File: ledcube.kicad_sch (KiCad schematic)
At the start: 0 parts

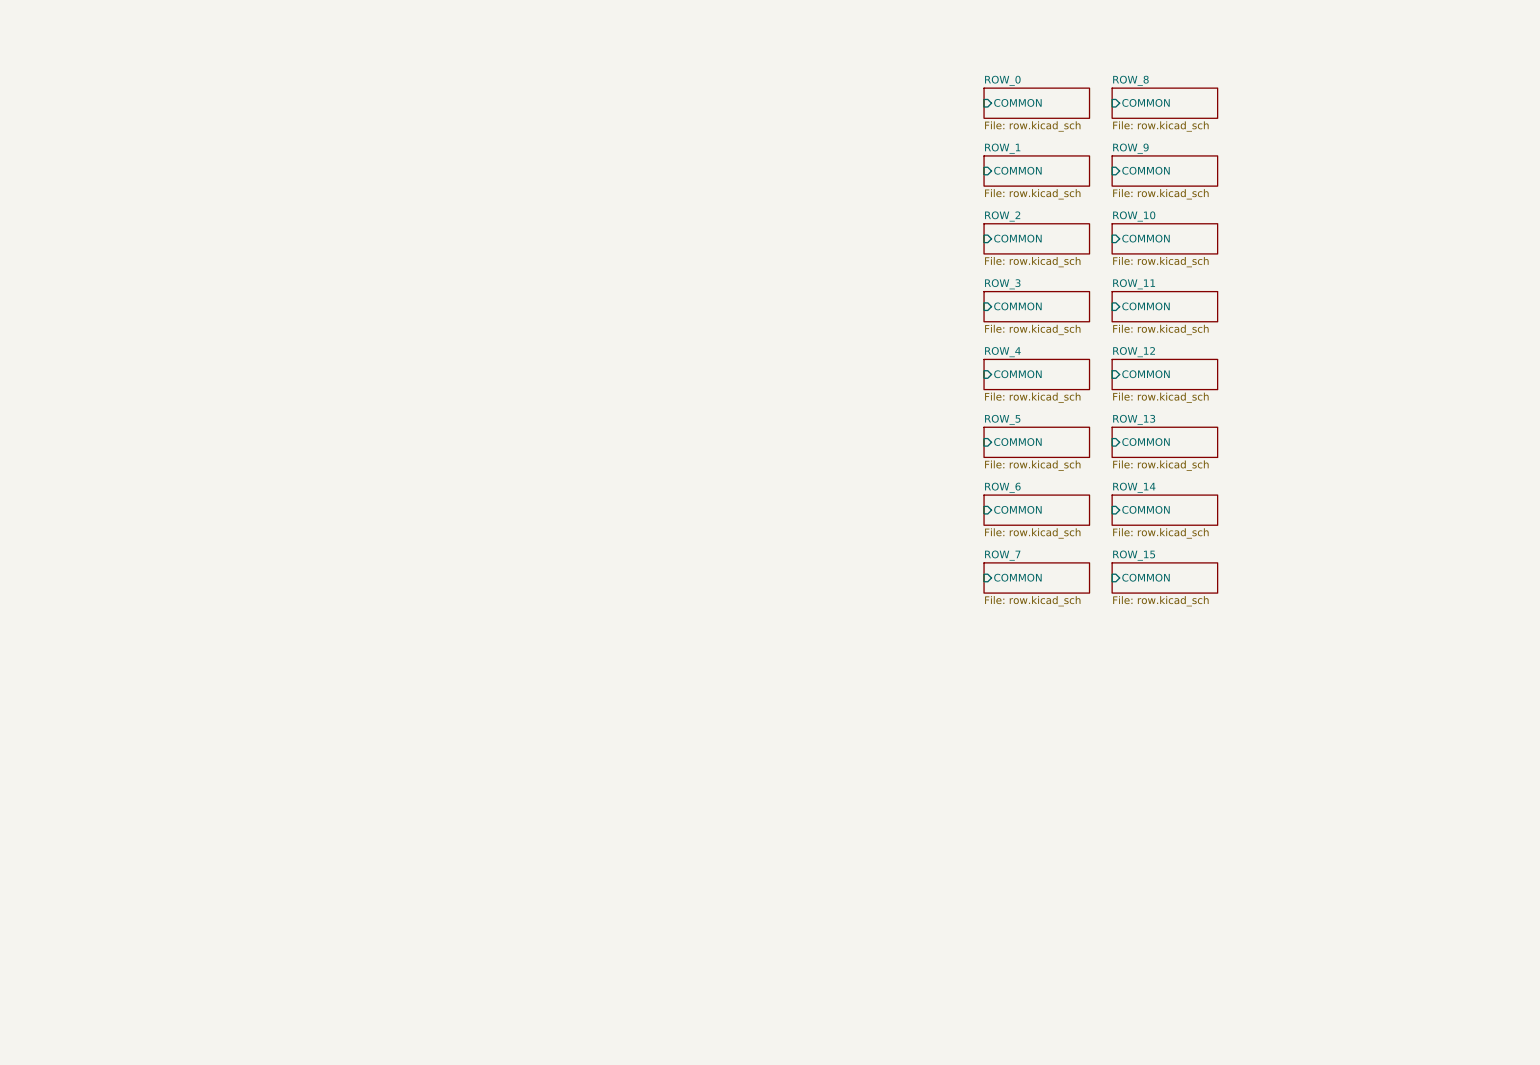
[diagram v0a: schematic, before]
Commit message: Row/column labels attached to shift registers/drivers
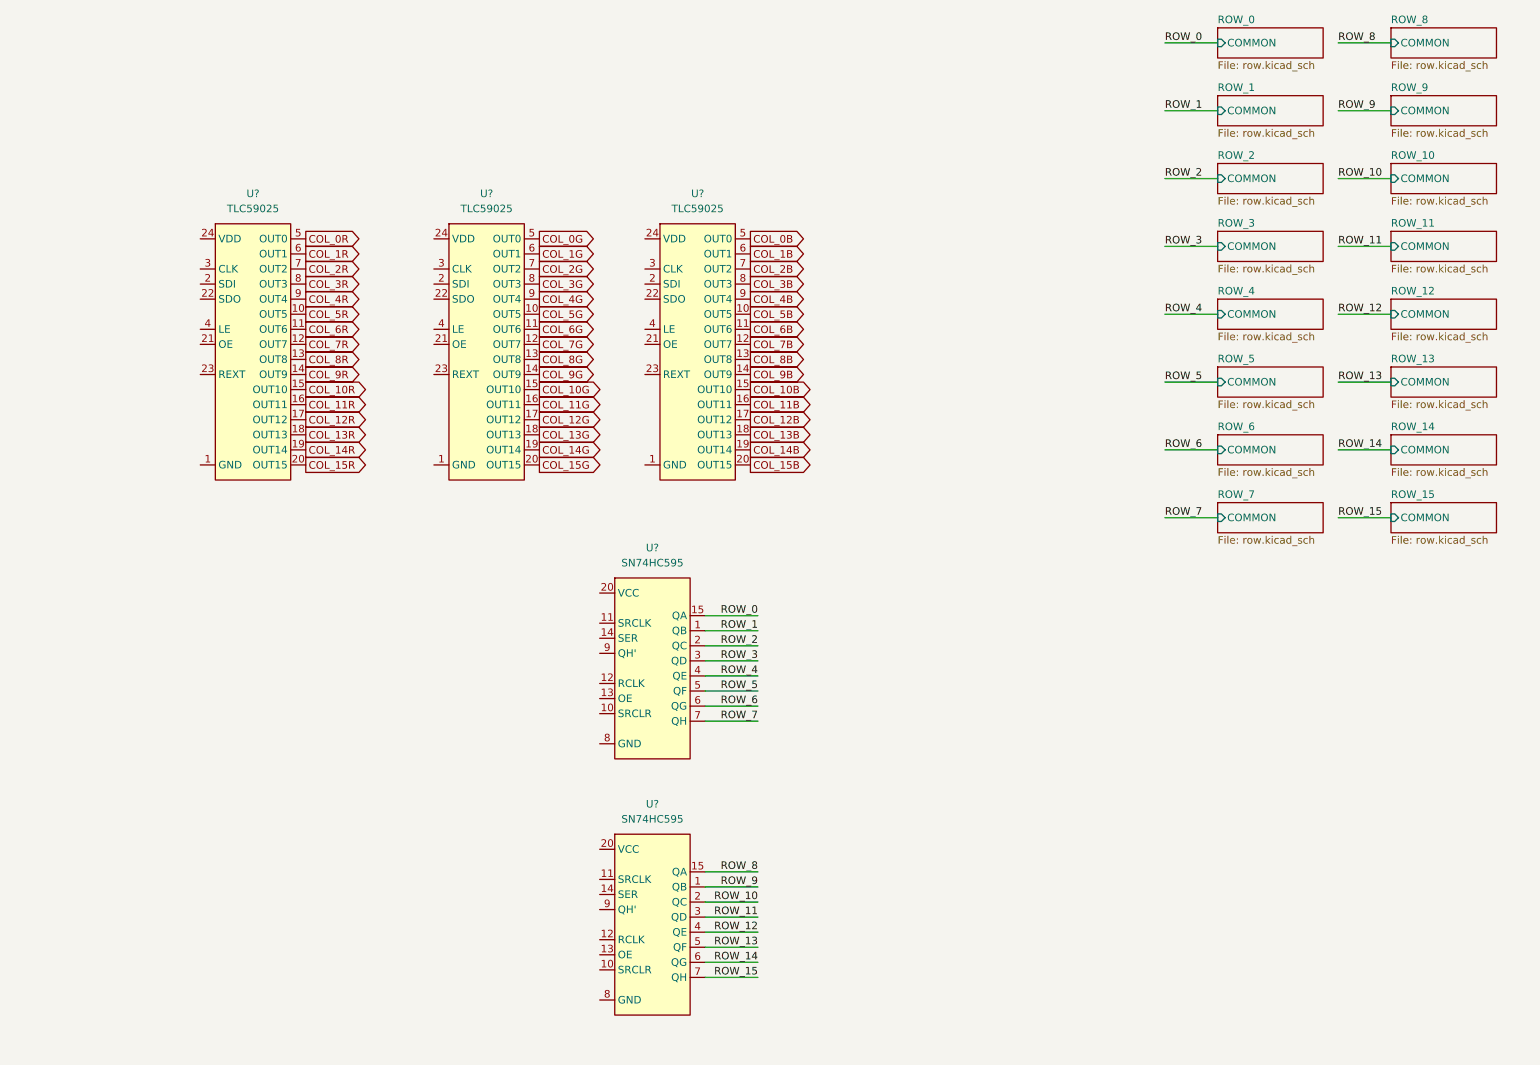
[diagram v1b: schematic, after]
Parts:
- added U? (x2): SN74HC595, symbol ledcube:SN74HC595
- added U? (x3): TLC59025, symbol ledcube:TLC59025
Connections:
- new net COL_0B: U?.5 (OUT0)
- new net COL_0G: U?.5 (OUT0)
- new net COL_0R: U?.5 (OUT0)
- new net COL_10B: U?.15 (OUT10)
- new net COL_10G: U?.15 (OUT10)
- new net COL_10R: U?.15 (OUT10)
- new net COL_11B: U?.16 (OUT11)
- new net COL_11G: U?.16 (OUT11)
- new net COL_11R: U?.16 (OUT11)
- new net COL_12B: U?.17 (OUT12)
- new net COL_12G: U?.17 (OUT12)
- new net COL_12R: U?.17 (OUT12)
- new net COL_13B: U?.18 (OUT13)
- new net COL_13G: U?.18 (OUT13)
- new net COL_13R: U?.18 (OUT13)
- new net COL_14B: U?.19 (OUT14)
- new net COL_14G: U?.19 (OUT14)
- new net COL_14R: U?.19 (OUT14)
- new net COL_15B: U?.20 (OUT15)
- new net COL_15G: U?.20 (OUT15)
- new net COL_15R: U?.20 (OUT15)
- new net COL_1B: U?.6 (OUT1)
- new net COL_1G: U?.6 (OUT1)
- new net COL_1R: U?.6 (OUT1)
- new net COL_2B: U?.7 (OUT2)
- new net COL_2G: U?.7 (OUT2)
- new net COL_2R: U?.7 (OUT2)
- new net COL_3B: U?.8 (OUT3)
- new net COL_3G: U?.8 (OUT3)
- new net COL_3R: U?.8 (OUT3)
- new net COL_4B: U?.9 (OUT4)
- new net COL_4G: U?.9 (OUT4)
- new net COL_4R: U?.9 (OUT4)
- new net COL_5B: U?.10 (OUT5)
- new net COL_5G: U?.10 (OUT5)
- new net COL_5R: U?.10 (OUT5)
- new net COL_6B: U?.11 (OUT6)
- new net COL_6G: U?.11 (OUT6)
- new net COL_6R: U?.11 (OUT6)
- new net COL_7B: U?.12 (OUT7)
- new net COL_7G: U?.12 (OUT7)
- new net COL_7R: U?.12 (OUT7)
- new net COL_8B: U?.13 (OUT8)
- new net COL_8G: U?.13 (OUT8)
- new net COL_8R: U?.13 (OUT8)
- new net COL_9B: U?.14 (OUT9)
- new net COL_9G: U?.14 (OUT9)
- new net COL_9R: U?.14 (OUT9)
- new net ROW_0: U?.15 (QA)
- new net ROW_1: U?.1 (QB)
- new net ROW_10: U?.2 (QC)
- new net ROW_11: U?.3 (QD)
- new net ROW_12: U?.4 (QE)
- new net ROW_13: U?.5 (QF)
- new net ROW_14: U?.6 (QG)
- new net ROW_15: U?.7 (QH)
- new net ROW_2: U?.2 (QC)
- new net ROW_3: U?.3 (QD)
- new net ROW_4: U?.4 (QE)
- new net ROW_5: U?.5 (QF)
- new net ROW_6: U?.6 (QG)
- new net ROW_7: U?.7 (QH)
- new net ROW_8: U?.15 (QA)
- new net ROW_9: U?.1 (QB)

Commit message: PMOS drivers, buffers, and serial connections
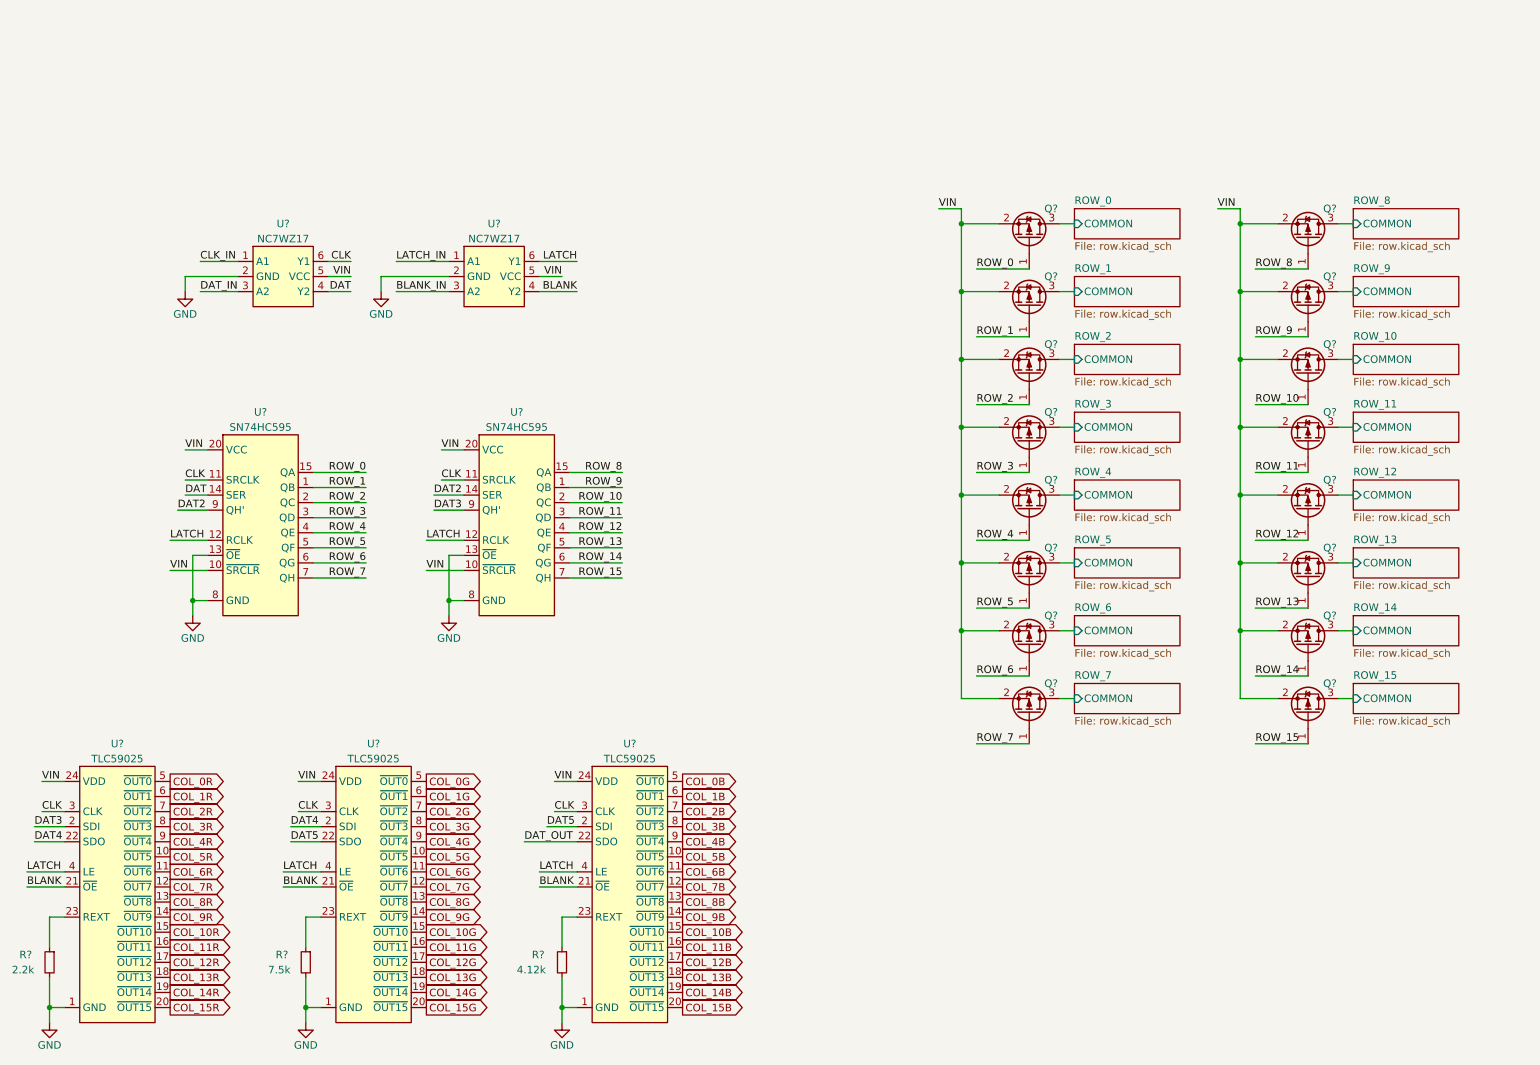
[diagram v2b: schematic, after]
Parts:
- added Q? (x16): Q_PMOS_GSD, symbol Device:Q_PMOS_GSD
- added R?: 7.5k, symbol Device:R_Small
- added R?: 2.2k, symbol Device:R_Small
- added R?: 4.12k, symbol Device:R_Small
- added U? (x2): NC7WZ17, Package_SON:Fairchild_MicroPak2-6_1.0x1.0mm_P0.35mm, symbol ledcube:NC7WZ17
- U? (x2): footprint (none) -> Package_SO:TSSOP-16_4.4x5mm_P0.65mm; MPN (none) -> SN74HC595PWR
- U? (x3): footprint (none) -> Package_SO:SSOP-24_3.9x8.7mm_P0.635mm; MPN (none) -> TLC59025IDBQR
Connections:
- net ROW_0: now also Q?.1 (G)
- net ROW_1: now also Q?.1 (G)
- net ROW_10: now also Q?.1 (G)
- net ROW_11: now also Q?.1 (G)
- net ROW_12: now also Q?.1 (G)
- net ROW_13: now also Q?.1 (G)
- net ROW_14: now also Q?.1 (G)
- net ROW_15: now also Q?.1 (G)
- net ROW_2: now also Q?.1 (G)
- net ROW_3: now also Q?.1 (G)
- net ROW_4: now also Q?.1 (G)
- net ROW_5: now also Q?.1 (G)
- net ROW_6: now also Q?.1 (G)
- net ROW_7: now also Q?.1 (G)
- net ROW_8: now also Q?.1 (G)
- net ROW_9: now also Q?.1 (G)
- net VIN: now reaches U?.10 (~{SRCLR})
- net VIN: now also U?.10 (~{SRCLR}), U?.20 (VCC), U?.20 (VCC), U?.24 (VDD), U?.24 (VDD), U?.24 (VDD), Q?.2 (S), Q?.2 (S), Q?.2 (S), Q?.2 (S), Q?.2 (S), Q?.2 (S), Q?.2 (S), Q?.2 (S), Q?.2 (S), Q?.2 (S), Q?.2 (S), Q?.2 (S), Q?.2 (S), Q?.2 (S), Q?.2 (S), Q?.2 (S), U?.5 (VCC), U?.5 (VCC)
- net CLK: now reaches U?.11 (SRCLK)
- net CLK: now also U?.11 (SRCLK), U?.3 (CLK), U?.3 (CLK), U?.3 (CLK), U?.6 (Y1)
- net LATCH: now reaches U?.12 (RCLK)
- net LATCH: now also U?.12 (RCLK), U?.4 (LE), U?.4 (LE), U?.4 (LE), U?.6 (Y1)
- net GND: now reaches U?.13 (~{OE})
- net GND: now also U?.1 (GND), U?.1 (GND), U?.1 (GND), U?.13 (~{OE}), U?.8 (GND), U?.8 (GND), R?.2, R?.2, R?.2, U?.2 (GND), U?.2 (GND)
- net DAT: now reaches U?.14 (SER)
- net DAT: now also U?.4 (Y2)
- net DAT2: now reaches U?.9 (QH')
- net DAT2: now also U?.14 (SER)
- net DAT4: now reaches U?.2 (SDI)
- net DAT4: now also U?.22 (SDO)
- net BLANK: now reaches U?.21 (~{OE})
- net BLANK: now also U?.21 (~{OE}), U?.21 (~{OE}), U?.4 (Y2)
- net DAT5: now reaches U?.22 (SDO)
- net DAT5: now also U?.2 (SDI)
- net at U?.23 (REXT): now also R?.1 (x3)
- net DAT3: now reaches U?.9 (QH')
- net DAT3: now also U?.2 (SDI)
- net DAT_OUT: now reaches U?.22 (SDO)
- new net BLANK_IN: U?.3 (A2)
- new net CLK_IN: U?.1 (A1)
- new net DAT_IN: U?.3 (A2)
- new net LATCH_IN: U?.1 (A1)
- new net ROW_0/COMMON: Q?.3 (D)
- new net ROW_1/COMMON: Q?.3 (D)
- new net ROW_10/COMMON: Q?.3 (D)
- new net ROW_11/COMMON: Q?.3 (D)
- new net ROW_12/COMMON: Q?.3 (D)
- new net ROW_13/COMMON: Q?.3 (D)
- new net ROW_14/COMMON: Q?.3 (D)
- new net ROW_15/COMMON: Q?.3 (D)
- new net ROW_2/COMMON: Q?.3 (D)
- new net ROW_3/COMMON: Q?.3 (D)
- new net ROW_4/COMMON: Q?.3 (D)
- new net ROW_5/COMMON: Q?.3 (D)
- new net ROW_6/COMMON: Q?.3 (D)
- new net ROW_7/COMMON: Q?.3 (D)
- new net ROW_8/COMMON: Q?.3 (D)
- new net ROW_9/COMMON: Q?.3 (D)
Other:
- moved on the sheet: U?

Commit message: Connectors and decoupling caps
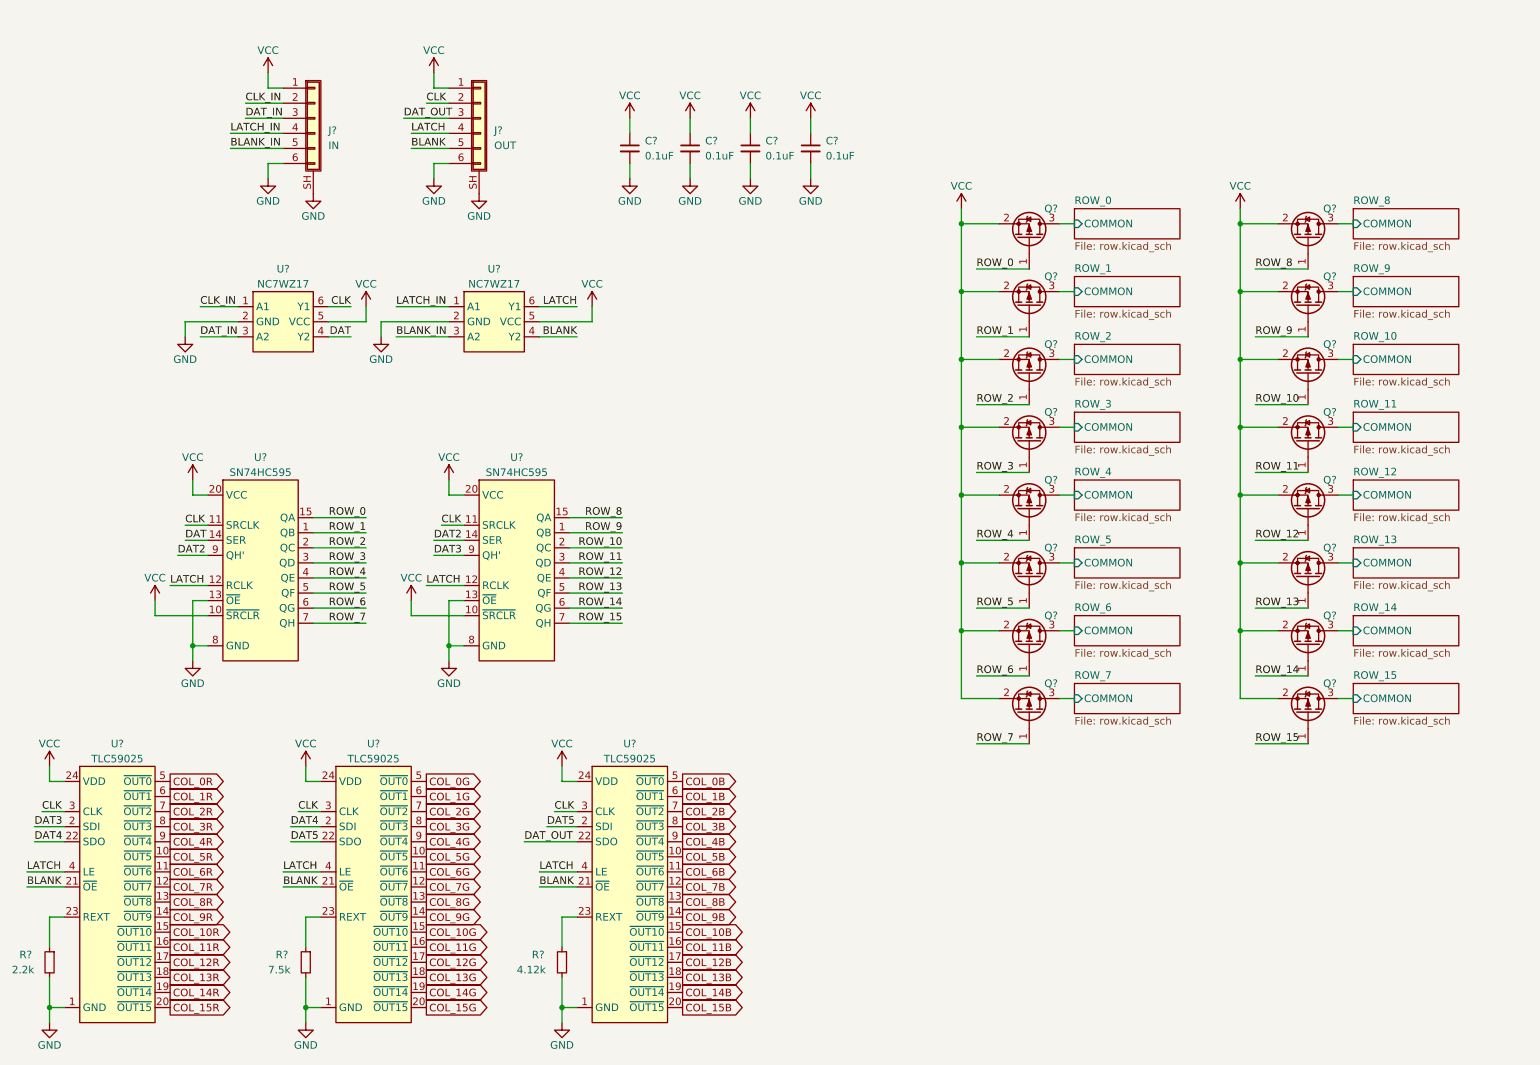
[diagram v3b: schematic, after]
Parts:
- added C? (x4): 0.1uF, symbol Device:C_Small
- added J?: IN, ledcube:5034800600, symbol Connector_Generic_Shielded:Conn_01x06_Shielded
- added J?: OUT, ledcube:5034800600, symbol Connector_Generic_Shielded:Conn_01x06_Shielded
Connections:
- net BLANK: now also J?.5 (Pin_5)
- net BLANK_IN: now also J?.5 (Pin_5)
- net CLK: now also J?.2 (Pin_2)
- net CLK_IN: now also J?.2 (Pin_2)
- net DAT_IN: now also J?.3 (Pin_3)
- net DAT_OUT: now also J?.3 (Pin_3)
- net GND: now also C?.2, C?.2, C?.2, C?.2, J?.6 (Pin_6), J?.6 (Pin_6), J?.SH (Shield), J?.SH (Shield)
- net LATCH: now also J?.4 (Pin_4)
- net LATCH_IN: now also J?.4 (Pin_4)
- net VIN renamed VCC
- net VCC: now also C?.1, C?.1, C?.1, C?.1, J?.1 (Pin_1), J?.1 (Pin_1)
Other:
- moved on the sheet: U?

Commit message: LED footprint
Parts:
- C? (x4): footprint (none) -> Capacitor_SMD:C_0603_1608Metric
- Q? (x16): footprint (none) -> Package_TO_SOT_SMD:SOT-883; MPN (none) -> LP0404N3T5G
- R? (x3): footprint (none) -> Resistor_SMD:R_0603_1608Metric
